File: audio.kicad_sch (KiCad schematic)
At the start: 6 parts, among them P1 PMOD_I2S, P2 PMOD_I2S

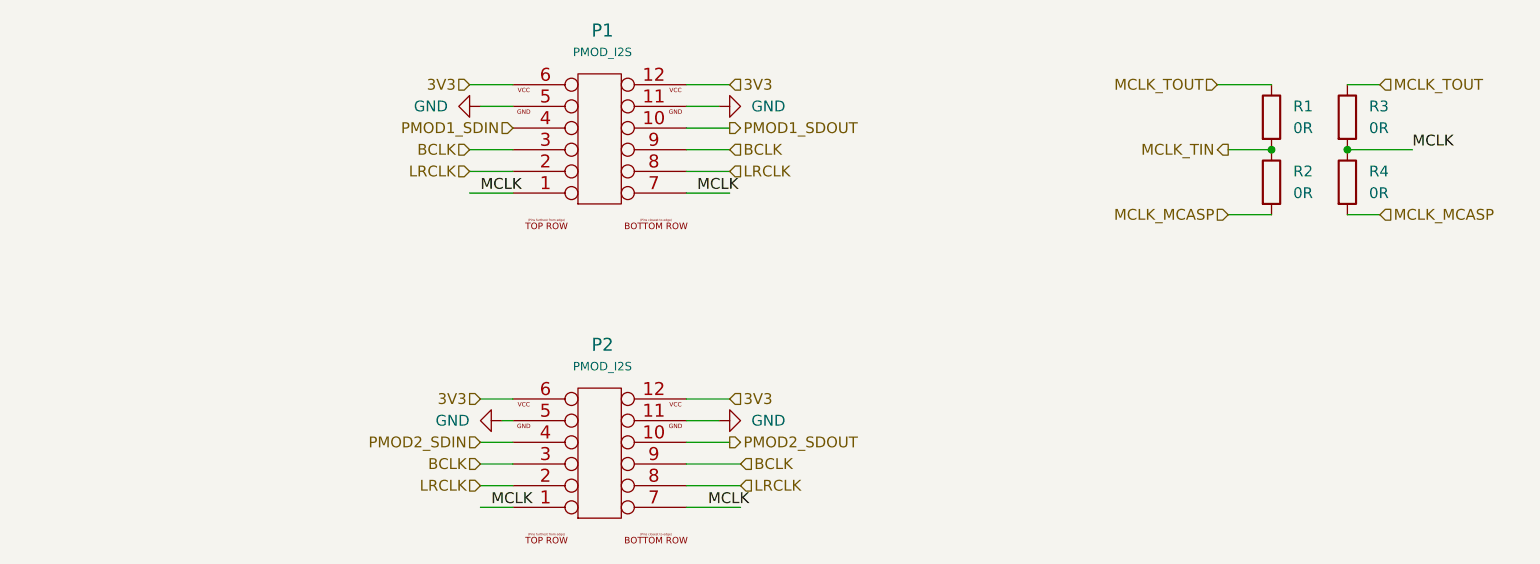
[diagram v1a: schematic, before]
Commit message: Migrate audio sheet to KL library symbols
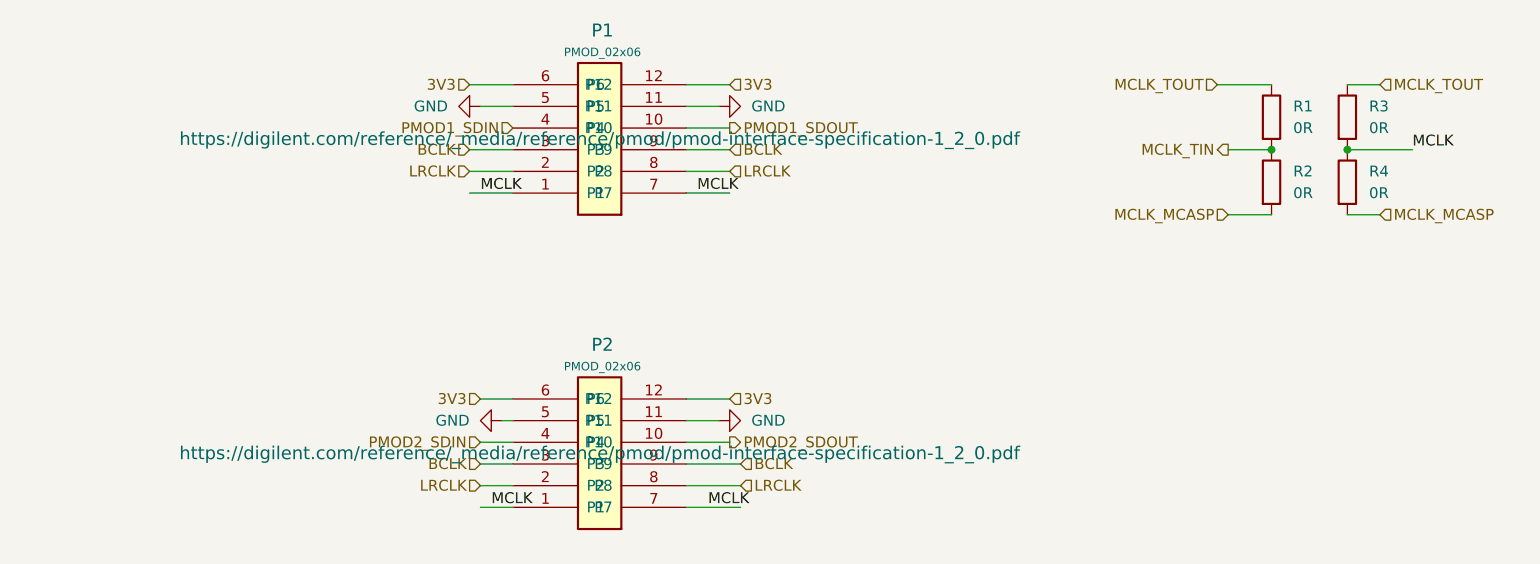
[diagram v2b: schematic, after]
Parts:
- P1, P2: value PMOD_I2S -> PMOD_02x06; footprint Connector_PinHeader_2.54mm:PinHeader_2x06_P2.54mm_Vertical_SMD -> KL_Footprints:06x02_2.54mm_SMD_Header; symbol pmod:PMOD-Device-x2-Type-Generic-Alt -> KL_Conn_Data:PMOD_02x06; Digikey (none) -> TBD; LCSC (none) -> TBD; MPN (none) -> TBD; Mouser (none) -> TBD
- R1, R2, R3, R4: footprint Resistor_SMD:R_0402_1005Metric_Pad0.72x0.64mm_HandSolder -> KL_Footprints:R_0402; symbol Device:R -> KL_R:R_0R_0.063W_5pct_0402; Digikey (none) -> TBD; LCSC (none) -> TBD; MPN (none) -> CRCW04020000Z0EDC; Mouser (none) -> 71-CRCW04020000Z0EDC; Package_in_inch (none) -> 0402; Power_in_W (none) -> 0.063; Tolerance_in_pct (none) -> 5

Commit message: Apply signal naming convention to all nets
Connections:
- net 3V3 renamed VDD_3V3
- net BCLK renamed I2S_BCLK_CPU_PMOD
- net LRCLK renamed I2S_LRCLK_CPU_PMOD
- net MCLK renamed MCLK_PMOD
- net PMOD1_SDIN renamed I2S_SDIN_CPU_to_PMOD1
- net PMOD1_SDOUT renamed I2S_SDOUT_PMOD1_to_CPU
- net PMOD2_SDIN renamed I2S_SDIN_CPU_to_PMOD2
- net PMOD2_SDOUT renamed I2S_SDOUT_PMOD2_to_CPU
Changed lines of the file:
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@@
 		)
 	)
-	(label "MCLK"
+	(label "MCLK_PMOD"
 		(at 40.64 55.88 0)
 		(effects
@@
 		)
 	)
-	(label "MCLK"
+	(label "MCLK_PMOD"
 		(at 149.86 50.8 0)
 		(effects
@@
 		)
 	)
-	(label "MCLK"
+	(label "MCLK_PMOD"
 		(at 66.04 55.88 0)
 		(effects
@@
 		)
 	)
-	(label "MCLK"
+	(label "MCLK_PMOD"
 		(at 41.91 92.71 0)
 		(effects
@@
 		)
 	)
-	(label "MCLK"
+	(label "MCLK_PMOD"
 		(at 67.31 92.71 0)
 		(effects
@@
 		)
 	)
-	(hierarchical_label "BCLK"
+	(hierarchical_label "I2S_BCLK_CPU_PMOD"
 		(shape input)
 		(at 40.64 87.63 180)
@@
 		)
 	)
-	(hierarchical_label "LRCLK"
+	(hierarchical_label "I2S_LRCLK_CPU_PMOD"
 		(shape input)
 		(at 71.12 90.17 0)
@@
 		)
 	)
-	(hierarchical_label "3V3"
+	(hierarchical_label "VDD_3V3"
 		(shape input)
 		(at 40.64 80.01 180)
@@
 		)
 	)
-	(hierarchical_label "3V3"
+	(hierarchical_label "VDD_3V3"
 		(shape input)
 		(at 69.85 80.01 0)
@@
 		)
 	)
-	(hierarchical_label "PMOD2_SDOUT"
+	(hierarchical_label "I2S_SDOUT_PMOD2_to_CPU"
 		(shape output)
 		(at 69.85 85.09 0)
@@
 		)
 	)
-	(hierarchical_label "PMOD1_SDIN"
+	(hierarchical_label "I2S_SDIN_CPU_to_PMOD1"
 		(shape input)
 		(at 44.45 48.26 180)
@@
 		)
 	)
-	(hierarchical_label "BCLK"
+	(hierarchical_label "I2S_BCLK_CPU_PMOD"
 		(shape input)
 		(at 71.12 87.63 0)
@@
 		)
 	)
-	(hierarchical_label "PMOD1_SDOUT"
+	(hierarchical_label "I2S_SDOUT_PMOD1_to_CPU"
 		(shape output)
 		(at 69.85 48.26 0)
@@
 		)
 	)
-	(hierarchical_label "3V3"
+	(hierarchical_label "VDD_3V3"
 		(shape input)
 		(at 39.37 43.18 180)
@@
 		)
 	)
-	(hierarchical_label "BCLK"
+	(hierarchical_label "I2S_BCLK_CPU_PMOD"
 		(shape input)
 		(at 69.85 50.8 0)
@@
 		)
 	)
-	(hierarchical_label "LRCLK"
+	(hierarchical_label "I2S_LRCLK_CPU_PMOD"
 		(shape input)
 		(at 69.85 53.34 0)
@@
 		)
 	)
-	(hierarchical_label "LRCLK"
+	(hierarchical_label "I2S_LRCLK_CPU_PMOD"
 		(shape input)
 		(at 39.37 53.34 180)
@@
 		)
 	)
-	(hierarchical_label "BCLK"
+	(hierarchical_label "I2S_BCLK_CPU_PMOD"
 		(shape input)
 		(at 39.37 50.8 180)
@@
 		)
 	)
-	(hierarchical_label "LRCLK"
+	(hierarchical_label "I2S_LRCLK_CPU_PMOD"
 		(shape input)
 		(at 40.64 90.17 180)
@@
 		)
 	)
-	(hierarchical_label "3V3"
+	(hierarchical_label "VDD_3V3"
 		(shape input)
 		(at 69.85 43.18 0)
@@
 		)
 	)
-	(hierarchical_label "PMOD2_SDIN"
+	(hierarchical_label "I2S_SDIN_CPU_to_PMOD2"
 		(shape input)
 		(at 40.64 85.09 180)
